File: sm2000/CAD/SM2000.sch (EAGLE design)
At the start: 344 parts, among them CN1 HDR100-3, CN10 ST-3509, CN11 HDR100-3, CN2 JS-MU3-002, CN3 DS-0518, CN5 ST-3509, CN8 ST-3509, J1 JMP-2PIN, J2 JMP-2PIN, J3 JMP-2PIN, J4 CONN-BOOM-XH-2A, P10 TPAD50, P11 TPAD50, P12 TPAD50, P13 TPAD50, P14 TPAD50, P16 TPAD50, P18 TPAD50, P19 TPAD50, P20 TPAD50, P21 TPAD50, P3 TPAD50, P4 TPAD50, P5 TPAD50, P6 TPAD50, P7 TPAD50, P8 TPAD50, P9 TPAD50, Q1 MMBT3904, Q12 BRF92, Q13 BFQ19, Q14 RD01MUS2, Q17 MMT2904, Q18 MMT2904, Q2 MMBT3904, Q3 MMBT3904, Q4 MMBT3904, Q5 MMBT3904, Q6 MMBT3904, Q7 BC548, Q8 BC549, SW1 SW-LC2259, SW2 TS-026, SW3 SW-LC2259EENP, SW4 TS-026, SW5 TS-02B, U1 STM32F405VGT6, U10 DNL, U12 PGA-103+, U13 ADE-1, U2 LD3985M33R, U3 STMPS2141, U4 EMIF02-USB03F2, U5 TPS54329E, U7 SA612A, U8 LM386M-1, U9 LMV341, X1 BU-SMA-H, X2 BU-SMA-H

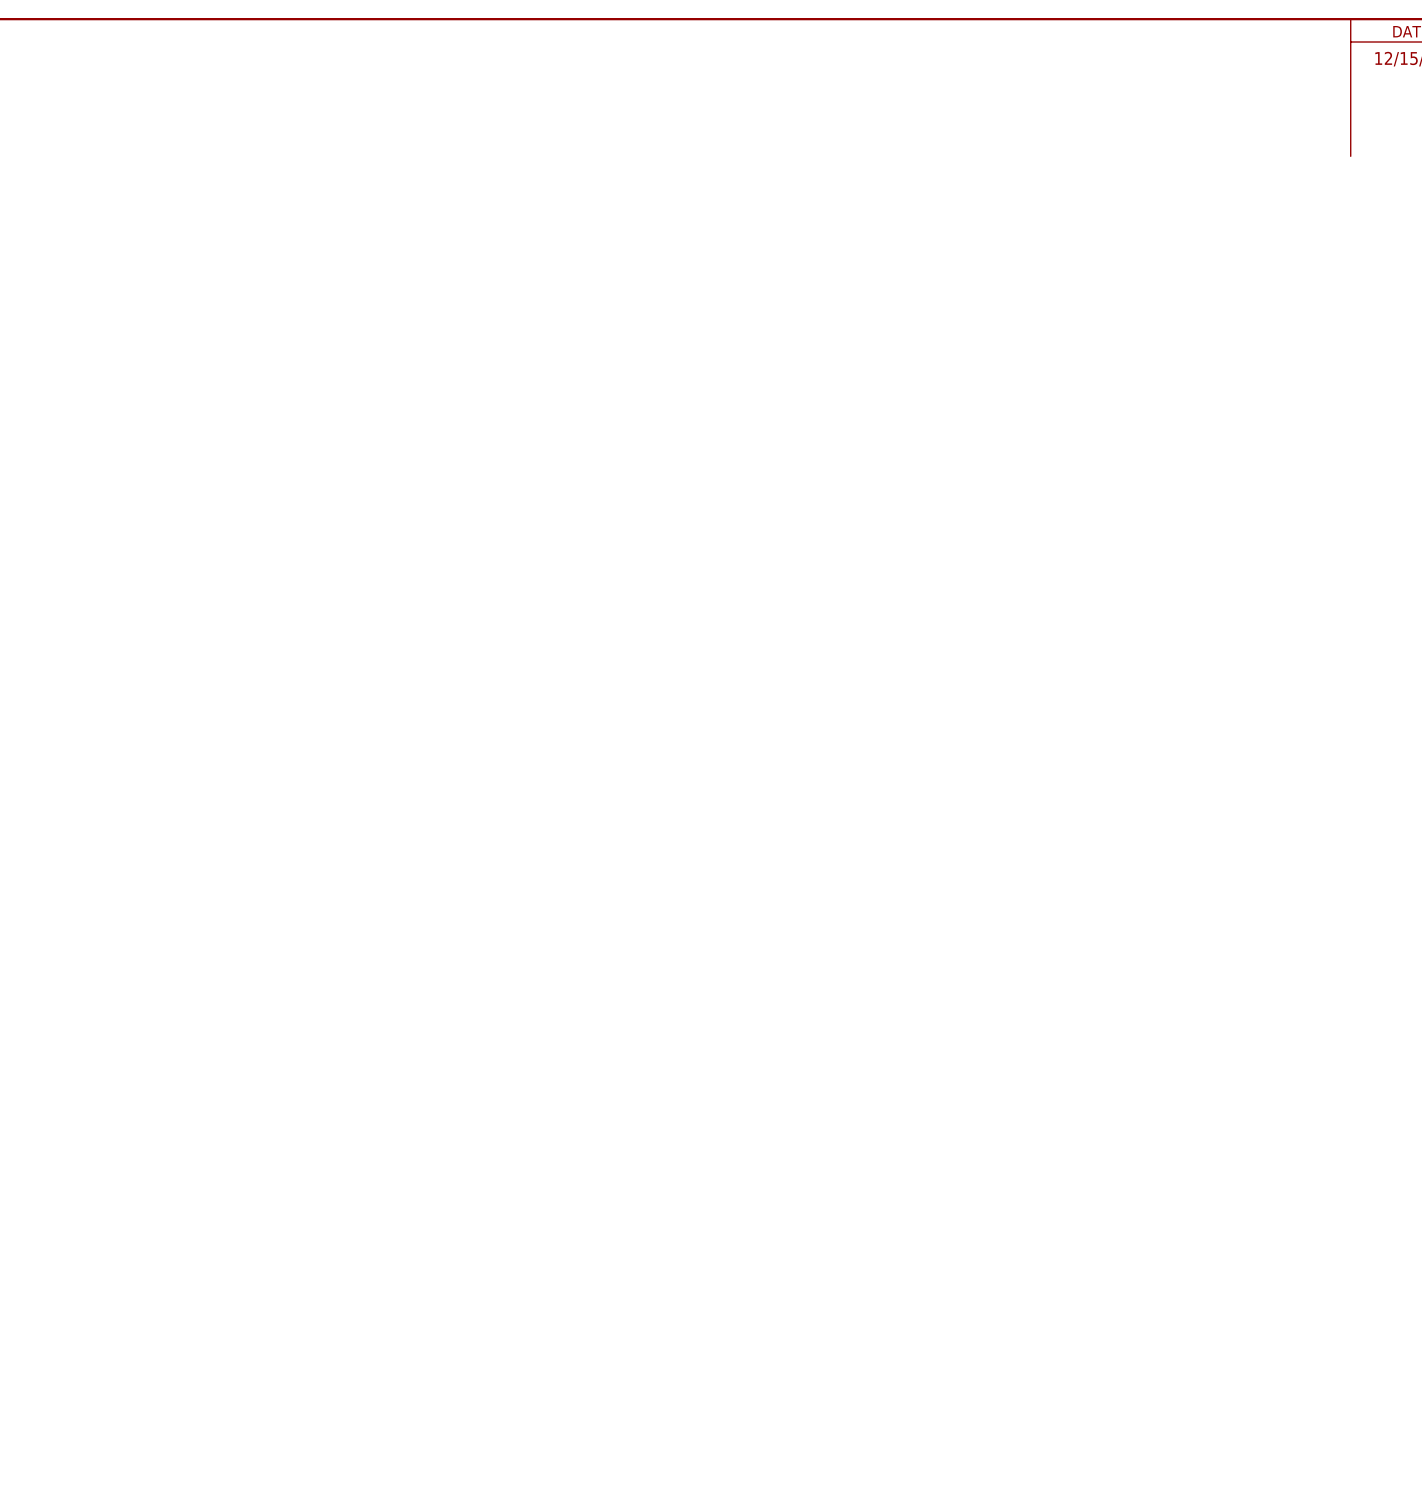
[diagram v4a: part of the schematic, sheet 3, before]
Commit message: aDDED lOCAL oSCILLATOR CIRCUITRY TO sm2000 sch. MOVED 3.3V PS TO SHT 4. CONTINUED SCHEMATIC CLEANUP RGB
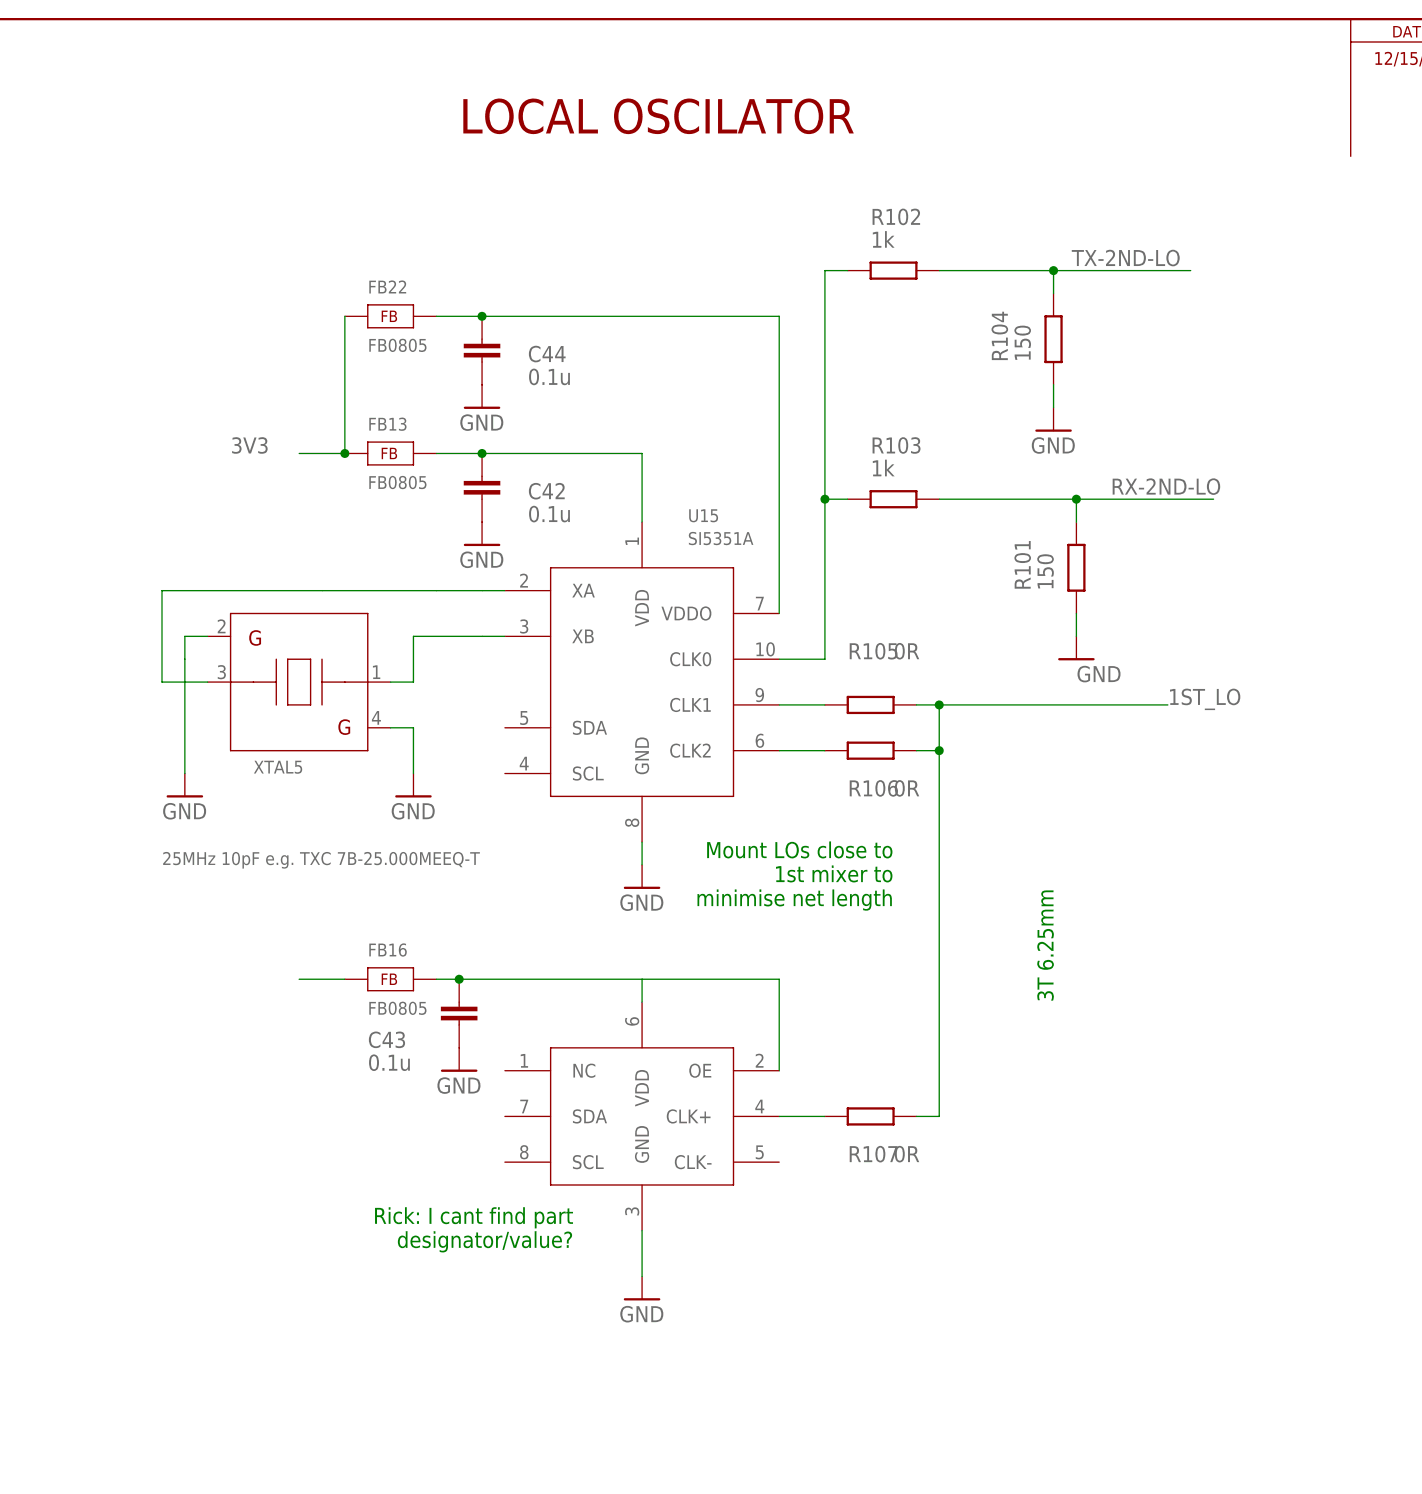
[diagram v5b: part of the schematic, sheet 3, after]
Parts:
- removed C4, C7: 100nF,25V, AA-ipc-7351-capacitor:CAPACITOR_0402
- removed C5, C6: 1uF,16V, AA-ipc-7351-capacitor:CAPACITOR_0603
- removed C8: 10nF,25V, AA-ipc-7351-capacitor:CAPACITOR_0402
- removed LED5: DNL, _RoweTel:SML-LX0603SRW
- removed R17: DNL, AA-ipc-7351-resistor:RESISTOR_0402
- removed R18: 0 Ohm, AA-ipc-7351-resistor:RESISTOR_0603
- removed U2: LD3985M33R, _RoweTel:LD3985
- added C36, C47: 1uF,16V, AA-ipc-7351-capacitor:CAPACITOR_0603
- added C38: 10nF,25V, AA-ipc-7351-capacitor:CAPACITOR_0402
- added C41, C45: 100nF,25V, AA-ipc-7351-capacitor:CAPACITOR_0402
- added C42, C43, C44: 0.1u, rcl:C-EU025-024X044
- added FB13, FB16, FB22: FB0805, _RoweTel:FB0805
- added LED6: DNL, _RoweTel:SML-LX0603SRW
- added R101, R104: 150, AA-ipc-7351-resistor:RESISTOR_0805
- added R102, R103: 1k, AA-ipc-7351-resistor:RESISTOR_0805
- added R105, R106, R107: 0R, AA-ipc-7351-resistor:RESISTOR_0805
- added R23: 0 Ohm, AA-ipc-7351-resistor:RESISTOR_0603
- added R9: DNL, AA-ipc-7351-resistor:RESISTOR_0402
- added U14: SI570CAC000141DG, _RoweTel:SI570
- added U15: SI5351A, _RoweTel:SI5351A
- added U6: LD3985M33R, _RoweTel:LD3985
- added XTAL5: 25MHz 10pF e.g. TXC 7B-25.000MEEQ-T, _RoweTel:XTAL-FY0800035
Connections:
- removed net N$12: C8.1, U2.BYBASS
- removed net N$19: LED5.A, R17.1
- new net 1ST_LO: R105.1, R106.1, R107.1
- new net 3V3: FB13.1, FB22.1
- new net N$117: FB16.1
- new net N$119: C43.1, FB16.2, U14.OE, U14.VDD
- new net N$120: C44.1, FB22.2, U15.VDDO
- new net N$121: R105.2, U15.CLK1
- new net N$122: R106.2, U15.CLK2
- new net N$123: R107.2, U14.CLK+
- new net N$124: R102.2, R103.2, U15.CLK0
- new net N$37: C38.1, U6.BYBASS
- new net N$52: LED6.A, R9.1
- new net N$63: C42.1, FB13.2, U15.VDD
- new net N$65: U15.XA, XTAL5.3
- new net N$80: U15.XB, XTAL5.1
- new net RX-2ND-LO: R101.1, R103.1
- new net TX-2ND-LO: R102.1, R104.1
- net +3.3V: now also C36.1, C41.1, R23.1, R9.2, U6.VOUT; no longer C4.1, C5.1, R17.2, R18.1, U2.VOUT
- net +5V: now also C45.1, C47.1, U6.INH, U6.VIN; no longer C6.1, C7.1, U2.INH, U2.VIN
- net GND: now also C36.2, C38.2, C41.2, C42.2, C43.2, C44.2, C45.2, C47.2, LED6.C, R101.2, R104.2, U14.GND, U15.GND, U6.GND, XTAL5.2, XTAL5.4; no longer C4.2, C5.2, C6.2, C7.2, C8.2, LED5.C, U2.GND
- net VDD: now also R23.2; no longer R18.2
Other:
- note added: "LOCAL OSCILATOR"
- note added: "Mount LOs close to 1st mixer to minimise net length"
- note added: "Rick: I cant find part designator/value?"
